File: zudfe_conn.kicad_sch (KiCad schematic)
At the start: 3 parts, among them J3 6469028-1, J4 6469028-1, J6 6469028-1

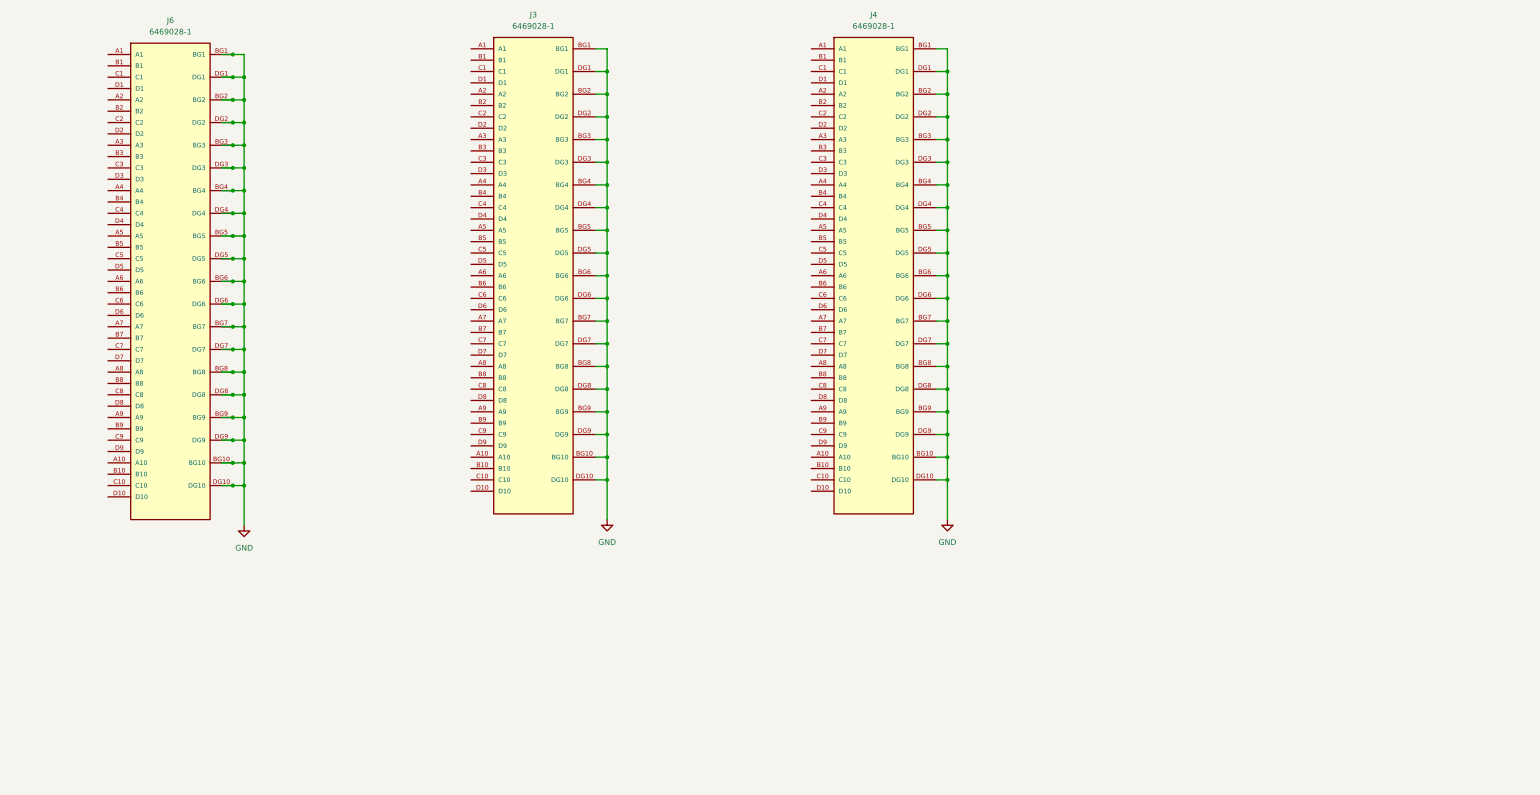
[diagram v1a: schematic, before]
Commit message: finish up regulator section
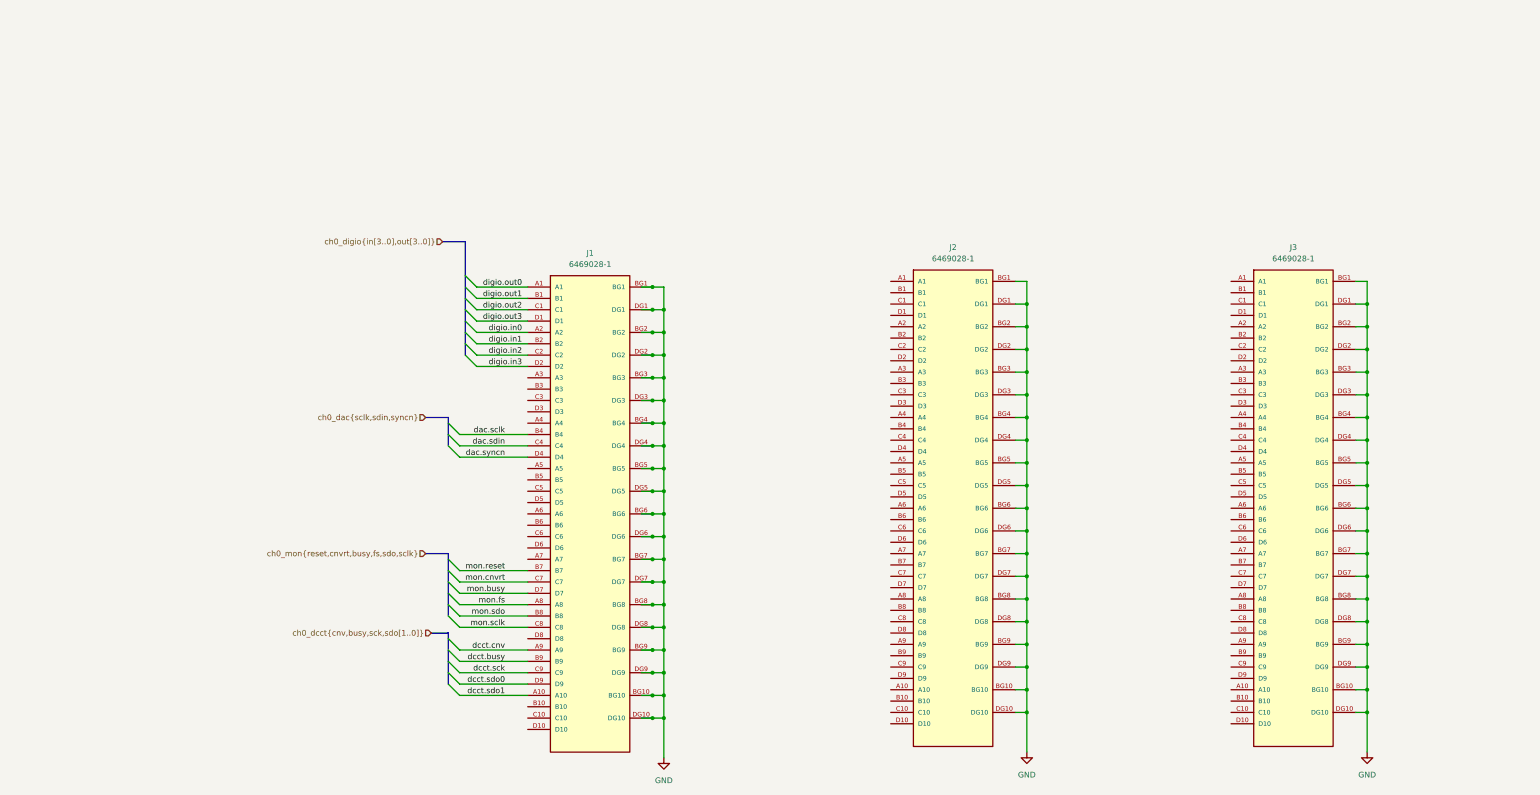
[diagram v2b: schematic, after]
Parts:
- renumbered J6 to J1, J3 to J2, J4 to J3
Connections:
- net digio.out0: now reaches J1.A1
- net dcct.sdo1: now reaches J1.A10
- net digio.in0: now reaches J1.A2
- net mon.fs: now reaches J1.A8
- net dcct.cnv: now reaches J1.A9
- net digio.out1: now reaches J1.B1
- net digio.in1: now reaches J1.B2
- net dac.sclk: now reaches J1.B4
- net mon.reset: now reaches J1.B7
- net mon.sdo: now reaches J1.B8
- net dcct.busy: now reaches J1.B9
- net digio.out2: now reaches J1.C1
- net digio.in2: now reaches J1.C2
- net dac.sdin: now reaches J1.C4
- net mon.cnvrt: now reaches J1.C7
- net mon.sclk: now reaches J1.C8
- net dcct.sck: now reaches J1.C9
- net digio.out3: now reaches J1.D1
- net digio.in3: now reaches J1.D2
- net dac.syncn: now reaches J1.D4
- net mon.busy: now reaches J1.D7
- net dcct.sdo0: now reaches J1.D9
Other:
- moved on the sheet: J1, J2, J3

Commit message: Add all 4 channels
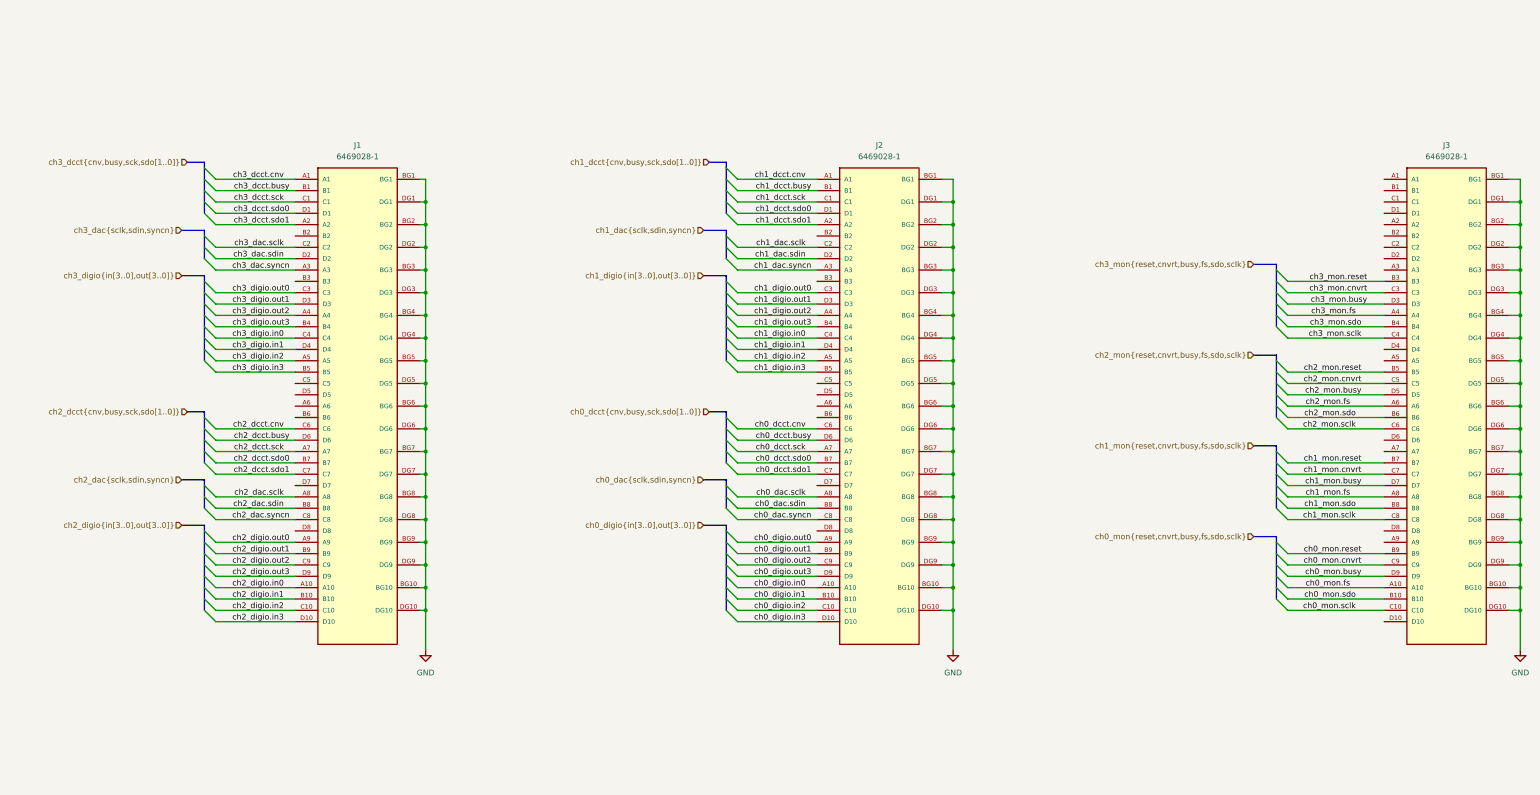
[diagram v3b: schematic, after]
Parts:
- renumbered J3 to J1, J1 to J3
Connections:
- net ch3_mon.fs: now reaches J3.A4
- net ch2_mon.fs: now reaches J3.A6
- net ch0_mon.sdo: now reaches J3.B10
- net ch3_mon.reset: now reaches J3.B3
- net ch2_mon.reset: now reaches J3.B5
- net ch2_mon.sdo: now reaches J3.B6
- net ch0_mon.sclk: now reaches J3.C10
- net ch3_mon.cnvrt: now reaches J3.C3
- net ch2_mon.cnvrt: now reaches J3.C5
- net ch2_mon.sclk: now reaches J3.C6
- net ch3_mon.busy: now reaches J3.D3
- net ch2_mon.busy: now reaches J3.D5
- net ch3_dcct.cnv: now reaches J1.A1
- net ch2_digio.in0: now reaches J1.A10
- net ch3_dcct.sdo1: now reaches J1.A2
- net ch3_dac.syncn: now reaches J1.A3
- net ch3_digio.out2: now reaches J1.A4
- net ch3_digio.in2: now reaches J1.A5
- net ch2_dcct.sck: now reaches J1.A7
- net ch2_dac.sclk: now reaches J1.A8
- net ch2_digio.out0: now reaches J1.A9
- net ch3_dcct.busy: now reaches J1.B1
- net ch2_digio.in1: now reaches J1.B10
- net ch3_digio.out3: now reaches J1.B4
- net ch3_digio.in3: now reaches J1.B5
- net ch2_dcct.sdo0: now reaches J1.B7
- net ch2_dac.sdin: now reaches J1.B8
- net ch2_digio.out1: now reaches J1.B9
- net ch3_dcct.sck: now reaches J1.C1
- net ch2_digio.in2: now reaches J1.C10
- net ch3_dac.sclk: now reaches J1.C2
- net ch3_digio.out0: now reaches J1.C3
- net ch3_digio.in0: now reaches J1.C4
- net ch2_dcct.cnv: now reaches J1.C6
- net ch2_dcct.sdo1: now reaches J1.C7
- net ch2_dac.syncn: now reaches J1.C8
- net ch2_digio.out2: now reaches J1.C9
- net ch3_dcct.sdo0: now reaches J1.D1
- net ch2_digio.in3: now reaches J1.D10
- net ch3_dac.sdin: now reaches J1.D2
- net ch3_digio.out1: now reaches J1.D3
- net ch3_digio.in1: now reaches J1.D4
- net ch2_dcct.busy: now reaches J1.D6
- net ch2_digio.out3: now reaches J1.D9
- net ch1_dcct.cnv: now reaches J2.A1
- net ch0_digio.in0: now reaches J2.A10
- net ch1_dcct.sdo1: now reaches J2.A2
- net ch1_dac.syncn: now reaches J2.A3
- net ch1_digio.out2: now reaches J2.A4
- net ch1_digio.in2: now reaches J2.A5
- net ch0_dcct.sck: now reaches J2.A7
- net ch0_dac.sclk: now reaches J2.A8
- net ch0_digio.out0: now reaches J2.A9
- net ch1_dcct.busy: now reaches J2.B1
- net ch0_digio.in1: now reaches J2.B10
- net ch1_digio.out3: now reaches J2.B4
- net ch1_digio.in3: now reaches J2.B5
- net ch0_dcct.sdo0: now reaches J2.B7
- net ch0_dac.sdin: now reaches J2.B8
- net ch0_digio.out1: now reaches J2.B9
- net ch1_dcct.sck: now reaches J2.C1
- net ch0_digio.in2: now reaches J2.C10
- net ch1_dac.sclk: now reaches J2.C2
- net ch1_digio.out0: now reaches J2.C3
- net ch1_digio.in0: now reaches J2.C4
- net ch0_dcct.cnv: now reaches J2.C6
- net ch0_dcct.sdo1: now reaches J2.C7
- net ch0_dac.syncn: now reaches J2.C8
- net ch0_digio.out2: now reaches J2.C9
- net ch1_dcct.sdo0: now reaches J2.D1
- net ch0_digio.in3: now reaches J2.D10
- net ch1_dac.sdin: now reaches J2.D2
- net ch1_digio.out1: now reaches J2.D3
- net ch1_digio.in1: now reaches J2.D4
- net ch0_dcct.busy: now reaches J2.D6
- net ch0_digio.out3: now reaches J2.D9
- net dac.sclk renamed ch3_mon.sdo
- net dac.sdin renamed ch3_mon.sclk
- net dac.syncn: no longer names the net of J3.D4
- net dcct.busy renamed ch0_mon.reset
- net dcct.cnv: no longer names the net of J3.A9
- net dcct.sck renamed ch0_mon.cnvrt
- net dcct.sdo0 renamed ch0_mon.busy
- net dcct.sdo1 renamed ch0_mon.fs
- net digio.in0: no longer names the net of J3.A2
- net digio.in1: no longer names the net of J3.B2
- net digio.in2: no longer names the net of J3.C2
- net digio.in3: no longer names the net of J3.D2
- net digio.out0: no longer names the net of J3.A1
- net digio.out1: no longer names the net of J3.B1
- net digio.out2: no longer names the net of J3.C1
- net digio.out3: no longer names the net of J3.D1
- net mon.busy renamed ch1_mon.busy
- net mon.cnvrt renamed ch1_mon.cnvrt
- net mon.fs renamed ch1_mon.fs
- net mon.reset renamed ch1_mon.reset
- net mon.sclk renamed ch1_mon.sclk
- net mon.sdo renamed ch1_mon.sdo
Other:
- moved on the sheet: J1, J2, J3

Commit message: Start routing
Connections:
- net ch0_mon.busy: now also J3.A9; no longer J3.D9
- net ch0_mon.cnvrt: now also J3.D8; no longer J3.C9
- net ch0_mon.fs: now also J3.B9; no longer J3.A10
- net ch0_mon.reset: now also J3.C8; no longer J3.B9
- net ch0_mon.sclk: now also J3.D9; no longer J3.C10
- net ch0_mon.sdo: now also J3.C9; no longer J3.B10
- net ch1_mon.busy: now also J3.A7; no longer J3.D7
- net ch1_mon.cnvrt: now also J3.D6; no longer J3.C7
- net ch1_mon.fs: now also J3.B7; no longer J3.A8
- net ch1_mon.reset: now also J3.C6; no longer J3.B7
- net ch1_mon.sclk: now also J3.D7; no longer J3.C8
- net ch1_mon.sdo: now also J3.C7; no longer J3.B8
- net ch2_mon.busy: now also J3.A5; no longer J3.D5
- net ch2_mon.cnvrt: now also J3.D4; no longer J3.C5
- net ch2_mon.fs: now also J3.B5; no longer J3.A6
- net ch2_mon.reset: now also J3.C4; no longer J3.B5
- net ch2_mon.sclk: now also J3.D5; no longer J3.C6
- net ch2_mon.sdo: now also J3.C5; no longer J3.B6
- net ch3_mon.busy: now also J3.A3; no longer J3.D3
- net ch3_mon.cnvrt: now also J3.D2; no longer J3.C3
- net ch3_mon.fs: now also J3.B3; no longer J3.A4
- net ch3_mon.reset: now also J3.C2; no longer J3.B3
- net ch3_mon.sclk: now also J3.D3; no longer J3.C4
- net ch3_mon.sdo: now also J3.C3; no longer J3.B4
- net dcct_flt_buf.12: now reaches J3.A1
- net dcct_flt_buf.34: now reaches J3.B1
- net dcct_flt_buf.56: now reaches J3.C1
- net dcct_flt_buf.78: now reaches J3.D1
- net i2c_scl: now reaches J3.D10
- new net i2c_sda: J3.C10
- no-connect marks 0 -> 21

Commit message: Finished layout
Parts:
- J1, J2, J3: Cost (none) -> 17.37; MFG (none) -> TE; MFG_PN (none) -> 6469028-1
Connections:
- net enb: now reaches J3.B10
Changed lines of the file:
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@@
 	(wire
 		(pts
+			(xy 283.21 168.91) (xy 337.82 168.91)
+		)
+		(stroke
+			(width 0)
+			(type default)
+		)
+	)
+	(wire
+		(pts
 			(xy 76.2 77.47) (xy 93.98 77.47)
 		)
@@
 		)
 	)
+	(hierarchical_label "enb"
+		(shape input)
+		(at 283.21 168.91 180)
+		(effects
+			(font
+				(size 1.27 1.27)
+			)
+			(justify right)
+		)
+	)
 	(hierarchical_label "ch1_dcct{cnv,busy,sck,sdo[1..0]}"
 		(shape input)
@@
 			)
 		)
-		(property "Description" ""
+		(property "Description" "CONN RCPT HIGH SPEED 60P EDGE MT"
 			(at 351.79 100.33 0)
 			(effects
@@
 			)
 		)
+		(property "Cost" "17.37"
+			(at 351.79 100.33 0)
+			(effects
+				(font
+					(size 1.27 1.27)
+				)
+				(hide yes)
+			)
+		)
+		(property "MFG" "TE"
+			(at 351.79 100.33 0)
+			(effects
+				(font
+					(size 1.27 1.27)
+				)
+				(hide yes)
+			)
+		)
+		(property "MFG_PN" "6469028-1"
+			(at 351.79 100.33 0)
+			(effects
+				(font
+					(size 1.27 1.27)
+				)
+				(hide yes)
+			)
+		)
 		(pin "DG1"
 		)
@@
 			)
 		)
-		(property "Description" ""
+		(property "Description" "CONN RCPT HIGH SPEED 60P EDGE MT"
 			(at 107.95 100.33 0)
 			(effects
@@
 			)
 		)
+		(property "Cost" "17.37"
+			(at 107.95 100.33 0)
+			(effects
+				(font
+					(size 1.27 1.27)
+				)
+				(hide yes)
+			)
+		)
+		(property "MFG" "TE"
+			(at 107.95 100.33 0)
+			(effects
+				(font
+					(size 1.27 1.27)
+				)
+				(hide yes)
+			)
+		)
+		(property "MFG_PN" "6469028-1"
+			(at 107.95 100.33 0)
+			(effects
+				(font
+					(size 1.27 1.27)
+				)
+				(hide yes)
+			)
+		)
 		(pin "DG1"
 		)
@@
 			)
 		)
-		(property "Description" ""
+		(property "Description" "CONN RCPT HIGH SPEED 60P EDGE MT"
 			(at 224.79 100.33 0)
 			(effects
@@
 				(hide yes)
 			)
+		)
+		(property "Cost" "17.37"
+			(at 224.79 100.33 0)
+			(effects
+				(font
+					(size 1.27 1.27)
+				)
+				(hide yes)
+			)
+		)
+		(property "MFG" "TE"
+			(at 224.79 100.33 0)
+			(effects
+				(font
+					(size 1.27 1.27)
+				)
+				(hide yes)
+			)
+		)
+		(property "MFG_PN" "6469028-1"
+			(at 224.79 100.33 0)
+			(effects
+				(font
+					(size 1.27 1.27)
+				)
+				(hide yes)
+			)
